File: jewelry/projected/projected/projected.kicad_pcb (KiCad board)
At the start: 2 copper layers, 28 x 28 mm, 46 parts, among them J1 TOUCH, J3 DOCK, J4 Leds, J5 SWD, J6 EXT, Q1 BC847CL, U1 STM32L432KBU6, U2 MCP73812T-420I-OT, U3 PCA9306DCUR, U4 MCP1640BT-I/CHY‎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

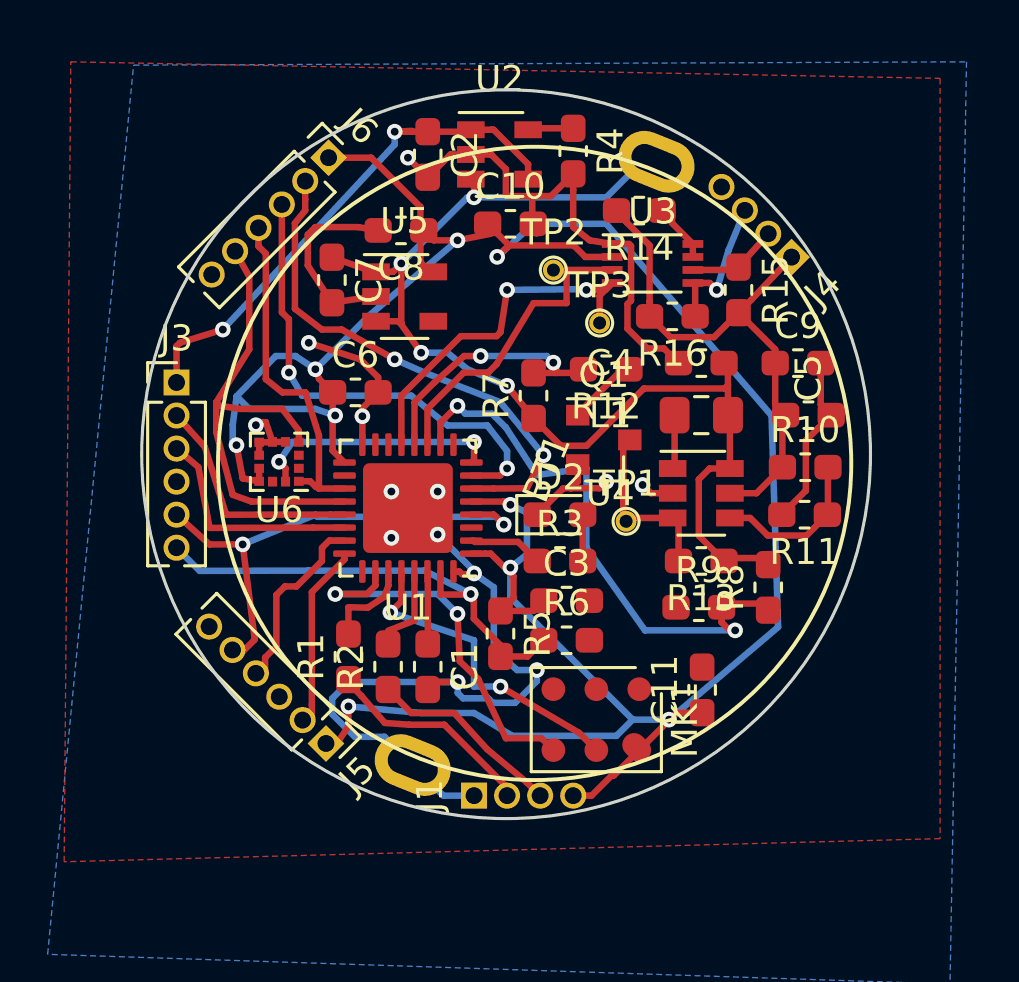
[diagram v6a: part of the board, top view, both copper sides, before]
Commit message: projected: Fix mic footprint and silkscreen
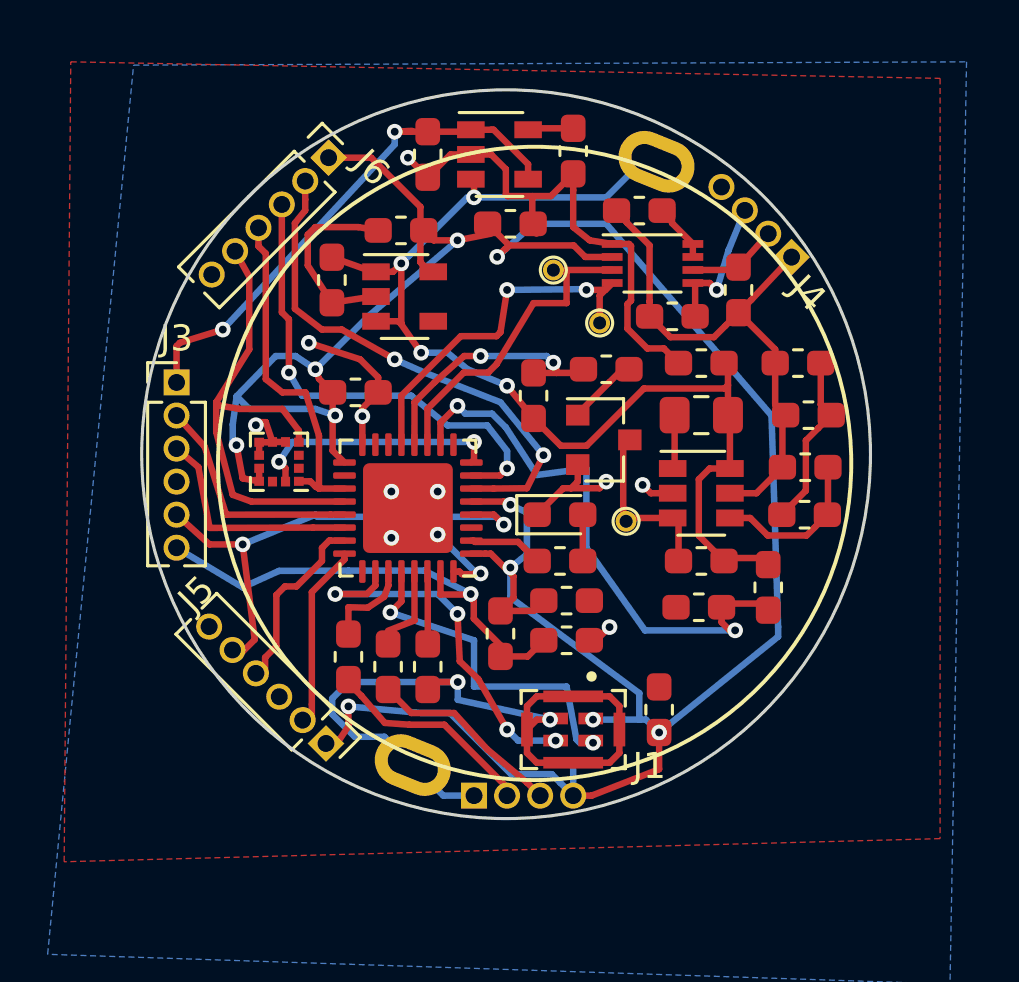
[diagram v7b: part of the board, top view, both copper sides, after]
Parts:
- removed MK1: MP45DT02, Sensor_Audio:ST_HLGA-6_3.76x4.72mm_P1.65mm
- added U7: MIC, projected:XDCR_CMM-4030DT-26154-TR, F.Cu at (52.6, 60.6)
- moved C11 1.82 mm to (55.9, 59.8)
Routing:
- net GND: track 69.1 -> 78.4 mm, vias 13 -> 14
- net VCC: track 106.4 -> 107.4 mm, vias 9 -> 10
- net /SAI_SD: track 12.4 -> 13.2 mm
- net /SAI_SCK: track 14.6 -> 14.3 mm, vias 2 -> 4
